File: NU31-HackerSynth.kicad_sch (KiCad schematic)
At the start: 134 parts, among them J1 Conn_02x07_Counter_Clockwise, J2 AudioJack3, J3 Barrel_Jack, J4 AudioJack2_SwitchT, J5 AudioJack2_SwitchT, J6 AudioJack2_SwitchT, Q1 NPN, Q2 NPN, Q3 NPN, Q4 NPN, SW1 SW_Push_DPDT, SW2 SW_SPDT, U1 LM358, U2 LM358, U3 LM358, U4 4017, U5 LM358, U6 LM358, U7 LM358

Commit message: Added eurorack power connector, assigned the footprints and made a (very) draft layout of the board
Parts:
- added J7: Eurorack Power, Connector_PinSocket_2.54mm:PinSocket_2x05_P2.54mm_Vertical, symbol Connector_Generic:Conn_02x05_Odd_Even
- C1, C6: value 50nf -> 50n; footprint (none) -> Capacitor_THT:C_Disc_D5.1mm_W3.2mm_P5.00mm
- C10, C14, C15, C16, C17, C18, C2, C5, C7: footprint (none) -> Capacitor_THT:C_Disc_D5.1mm_W3.2mm_P5.00mm
- C11, C12, C13: footprint (none) -> Capacitor_THT:CP_Radial_D5.0mm_P2.50mm
- C3: value 10nF -> 10n; footprint (none) -> Capacitor_THT:C_Disc_D5.1mm_W3.2mm_P5.00mm
- C4: value 10uF -> 10u; footprint (none) -> Capacitor_THT:C_Disc_D5.1mm_W3.2mm_P5.00mm
- C8: footprint (none) -> Diode_THT:D_A-405_P10.16mm_Horizontal
- C9: value 10 uF -> 10u; footprint (none) -> Capacitor_THT:CP_Radial_D5.0mm_P2.50mm
- D1, D10, D12, D14, D16, D18, D4, D6, D8: footprint (none) -> Diode_THT:D_A-405_P7.62mm_Horizontal
- D11, D13, D15, D17, D3, D5, D7, D9: footprint (none) -> LED_THT:LED_D3.0mm
- D2: value D -> 1N4001; footprint (none) -> Diode_THT:D_A-405_P10.16mm_Horizontal
- J1: footprint (none) -> Connector_PinHeader_2.54mm:PinHeader_2x08_P2.54mm_Vertical; symbol Connector_Generic:Conn_02x08_Counter_Clockwise -> Connector_Generic:Conn_02x08_Odd_Even
- J2: footprint (none) -> AudioJacks:Jack_3.5mm_QingPu_WQP-PJ366ST_Vertical
- J3: footprint (none) -> Connector_BarrelJack:BarrelJack_Wuerth_6941xx301002
- J4, J5, J6: footprint (none) -> AudioJacks:Jack_3.5mm_QingPu_WQP-PJ301M-12_Vertical
- JP1, JP2, JP3, JP4, JP5, JP6, JP7: footprint (none) -> Connector_PinHeader_2.54mm:PinHeader_1x02_P2.54mm_Vertical
- Q1, Q2, Q3, Q4: footprint (none) -> Package_TO_SOT_THT:TO-92L_Inline_Wide
- R1, R10, R11, R12, R13, R14, R15, R16, R17, R18, R19, R2, R20, R21, R22, R23, R24, R25, R26, R27, R28, R29, R3, R30, R31, R32, R33, R34, R35, R36, R37, R38, R39, R4, R40, R41, R42, R43, R44, R45, R46, R47, R48, R49, R5, R50, R51, R52, R53, R54, R55, R56, R57, R58, R6, R7, R8, R9: footprint (none) -> Resistor_THT:R_Axial_DIN0207_L6.3mm_D2.5mm_P10.16mm_Horizontal
- RV1, RV10, RV11, RV12, RV3: footprint (none) -> Potentiometer_THT:Potentiometer_Alpha_RD901F-40-00D_Single_Vertical
- RV13, RV14, RV4, RV5, RV6, RV7, RV8, RV9: footprint (none) -> Potentiometer_THT:Potentiometer_Bourns_PTA2043_Single_Slide
- RV2: footprint (none) -> Potentiometer_THT:Potentiometer_Bourns_3299P_Horizontal
- SW1: value SW_Push_DPDT -> SW_DPDT; footprint (none) -> Button_Switch_THT:SW_CK_JS202011CQN_DPDT_Straight
- SW2: footprint (none) -> Button_Switch_THT:SW_Slide_SPDT_Straight_CK_OS102011MS2Q
- U1, U2, U3, U5, U6, U7: footprint (none) -> Package_DIP:DIP-8_W7.62mm_Socket
- U4: value 4017 -> CD4017; footprint (none) -> Package_DIP:DIP-16_W7.62mm_Socket
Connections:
- net GND: now also J7.3 (Pin_3), J7.4 (Pin_4), J7.5 (Pin_5), J7.6 (Pin_6), J7.7 (Pin_7), J7.8 (Pin_8)
- net at R30.1, RV9.1, U4.1 (Q5): now also J1.10 (Pin_10); no longer J1.12 (Pin_12)
- net at R28.1, RV8.1, U4.10 (Q4): now also J1.8 (Pin_8); no longer J1.13 (Pin_13)
- net at J1.1 (Pin_1), J1.3 (Pin_3), J1.5 (Pin_5)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: now also J1.11 (Pin_11), J1.13 (Pin_13), J1.15 (Pin_15), J1.9 (Pin_9); no longer J1.2 (Pin_2), J1.4 (Pin_4), J1.6 (Pin_6), J1.8 (Pin_8)
- net at R8.1, RV5.1, U4.2 (Q1): now also J1.2 (Pin_2); no longer J1.16 (Pin_16)
- net at R24.1, RV6.1, U4.4 (Q2): now also J1.4 (Pin_4); no longer J1.15 (Pin_15)
- net at R53.1, RV13.1, U4.5 (Q6): now also J1.12 (Pin_12); no longer J1.11 (Pin_11)
- net at R55.1, RV14.1, U4.6 (Q7): now also J1.14 (Pin_14); no longer J1.10 (Pin_10)
- net at R26.1, RV7.1, U4.7 (Q3): now also J1.6 (Pin_6); no longer J1.14 (Pin_14)
- net at U4.9 (Q8): now also J1.16 (Pin_16); no longer J1.9 (Pin_9)
- net at D2.2 (A), J3.2: now also J7.10 (Pin_10), J7.9 (Pin_9)
- no-connect marks 4 -> 6
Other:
- moved on the sheet: C13, D2, J3

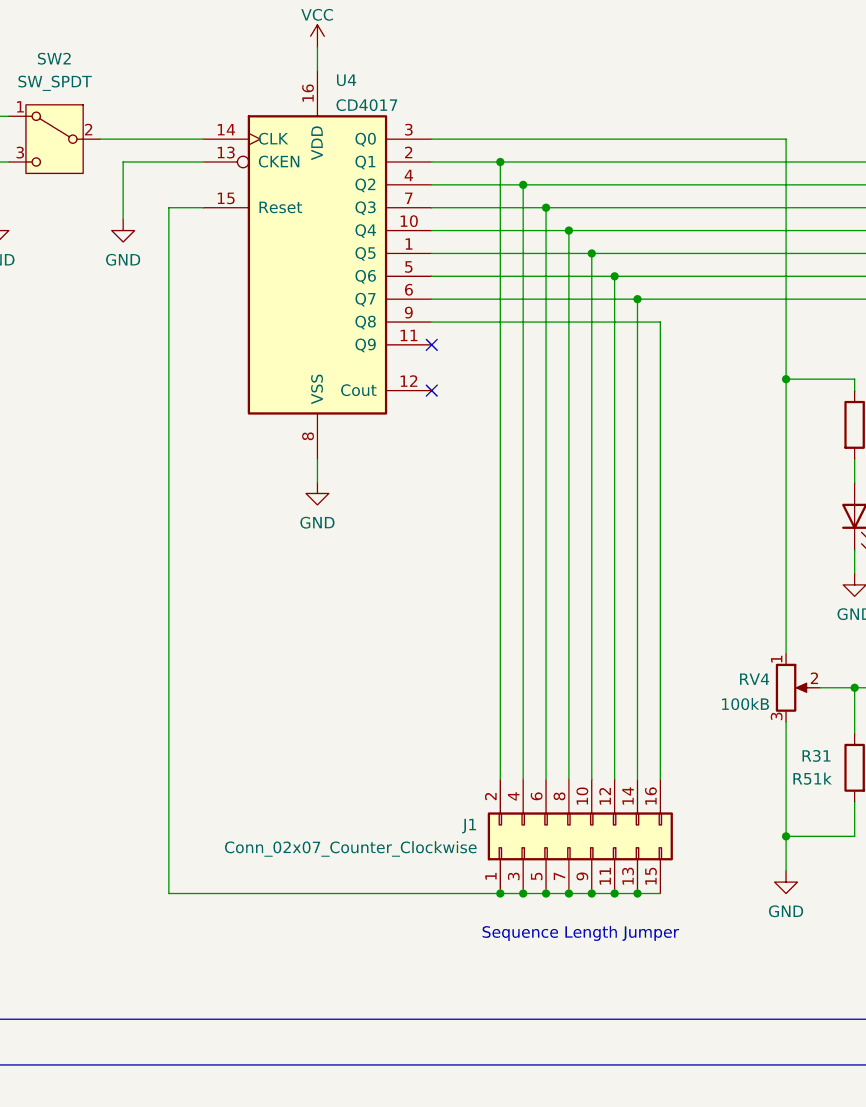
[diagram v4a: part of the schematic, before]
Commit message: Replaced sequence length jumper pins with 8-position switch
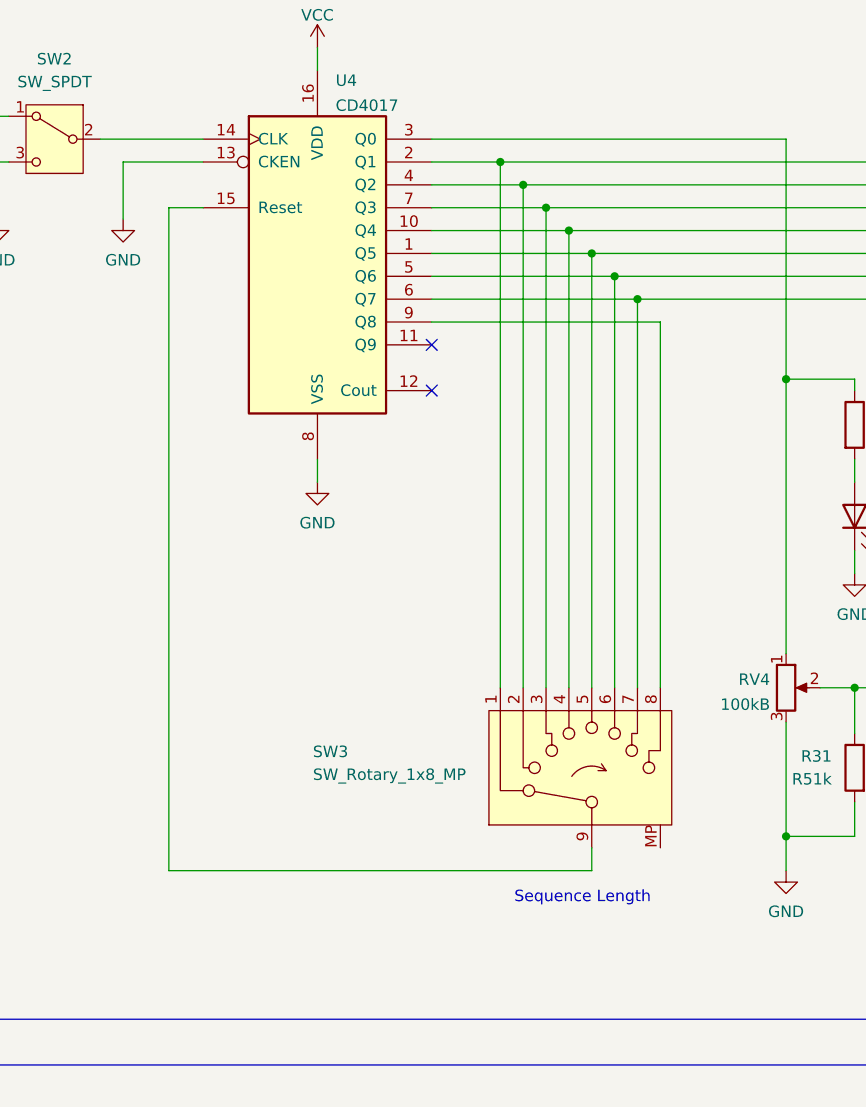
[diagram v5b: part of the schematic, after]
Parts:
- removed J1: Conn_02x07_Counter_Clockwise, Connector_PinHeader_2.54mm:PinHeader_2x08_P2.54mm_Vertical, symbol Connector_Generic:Conn_02x08_Odd_Even
- added SW3: SW_Rotary_1x8_MP, symbol Switch:SW_Rotary_1x8_MP
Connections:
- net at R30.1, RV9.1, U4.1 (Q5): now also SW3.5
- net at R28.1, RV8.1, U4.10 (Q4): now also SW3.4
- net at U4.15 (Reset): now also SW3.9
- net at R8.1, RV5.1, U4.2 (Q1): now also SW3.1
- net at R24.1, RV6.1, U4.4 (Q2): now also SW3.2
- net at R53.1, RV13.1, U4.5 (Q6): now also SW3.6
- net at R55.1, RV14.1, U4.6 (Q7): now also SW3.7
- net at R26.1, RV7.1, U4.7 (Q3): now also SW3.3
- net at U4.9 (Q8): now also SW3.8
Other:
- note added: "Sequence Length"
- note removed: "Sequence Length Jumper"
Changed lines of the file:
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@@
 		)
 	)
-	(text "Sequence Length Jumper"
+	(text "Sequence Length"
 		(exclude_from_sim no)
-		(at 100.33 446.532 0)
+		(at 100.584 442.468 0)
 		(effects
 			(font
@@
 	)
 	(junction
-		(at 106.68 441.96)
-		(diameter 0)
-		(color 0 0 0 0)
-	)
-	(junction
 		(at 327.66 513.08)
 		(diameter 0)
@@
 	)
 	(junction
-		(at 91.44 441.96)
-		(diameter 0)
-		(color 0 0 0 0)
-	)
-	(junction
 		(at 363.22 254)
 		(diameter 0)
@@
 	)
 	(junction
-		(at 96.52 441.96)
-		(diameter 0)
-		(color 0 0 0 0)
-	)
-	(junction
 		(at 123.19 384.81)
 		(diameter 0)
@@
 	)
 	(junction
-		(at 101.6 441.96)
-		(diameter 0)
-		(color 0 0 0 0)
-	)
-	(junction
 		(at 162.56 175.26)
 		(diameter 0)
@@
 	)
 	(junction
-		(at 99.06 441.96)
-		(diameter 0)
-		(color 0 0 0 0)
-	)
-	(junction
 		(at 92.71 285.75)
 		(diameter 0)
@@
 	)
 	(junction
-		(at 104.14 441.96)
-		(diameter 0)
-		(color 0 0 0 0)
-	)
-	(junction
 		(at 342.9 73.66)
 		(diameter 0)
@@
 	)
 	(junction
-		(at 93.98 441.96)
-		(diameter 0)
-		(color 0 0 0 0)
-	)
-	(junction
 		(at 74.93 502.92)
 		(diameter 0)
@@
 	(wire
 		(pts
-			(xy 101.6 441.96) (xy 104.14 441.96)
-		)
-		(stroke
-			(width 0)
-			(type default)
-		)
-	)
-	(wire
-		(pts
 			(xy 341.63 60.96) (xy 342.9 60.96)
 		)
@@
 	(wire
 		(pts
+			(xy 137.16 431.8) (xy 137.16 445.77)
+		)
+		(stroke
+			(width 0)
+			(type default)
+		)
+	)
+	(wire
+		(pts
 			(xy 80.01 285.75) (xy 92.71 285.75)
 		)
@@
 	(wire
 		(pts
-			(xy 99.06 368.3) (xy 99.06 429.26)
+			(xy 99.06 368.3) (xy 99.06 419.1)
 		)
 		(stroke
@@
 	(wire
 		(pts
-			(xy 93.98 363.22) (xy 93.98 429.26)
+			(xy 93.98 363.22) (xy 93.98 419.1)
 		)
 		(stroke
@@
 	(wire
 		(pts
-			(xy 91.44 441.96) (xy 54.61 441.96)
+			(xy 54.61 439.42) (xy 101.6 439.42)
 		)
 		(stroke
@@
 	(wire
 		(pts
-			(xy 96.52 441.96) (xy 99.06 441.96)
-		)
-		(stroke
-			(width 0)
-			(type default)
-		)
-	)
-	(wire
-		(pts
 			(xy 36.83 546.1) (xy 36.83 547.37)
 		)
@@
 	(wire
 		(pts
-			(xy 91.44 441.96) (xy 93.98 441.96)
-		)
-		(stroke
-			(width 0)
-			(type default)
-		)
-	)
-	(wire
-		(pts
 			(xy 340.36 488.95) (xy 345.44 488.95)
 		)
@@
 	(wire
 		(pts
-			(xy 137.16 431.8) (xy 137.16 445.77)
-		)
-		(stroke
-			(width 0)
-			(type default)
-		)
-	)
-	(wire
-		(pts
 			(xy 300.99 53.34) (xy 300.99 68.58)
 		)
@@
 	(wire
 		(pts
+			(xy 101.6 439.42) (xy 101.6 436.88)
+		)
+		(stroke
+			(width 0)
+			(type default)
+		)
+	)
+	(wire
+		(pts
 			(xy 83.82 375.92) (xy 106.68 375.92)
 		)
@@
 	(wire
 		(pts
-			(xy 91.44 360.68) (xy 91.44 429.26)
+			(xy 91.44 360.68) (xy 91.44 419.1)
 		)
 		(stroke
@@
 	(wire
 		(pts
-			(xy 93.98 441.96) (xy 96.52 441.96)
-		)
-		(stroke
-			(width 0)
-			(type default)
-		)
-	)
-	(wire
-		(pts
 			(xy 358.14 419.1) (xy 358.14 424.18)
 		)
@@
 	(wire
 		(pts
-			(xy 106.68 375.92) (xy 106.68 429.26)
+			(xy 106.68 375.92) (xy 106.68 419.1)
 		)
 		(stroke
@@
 	(wire
 		(pts
-			(xy 106.68 441.96) (xy 109.22 441.96)
-		)
-		(stroke
-			(width 0)
-			(type default)
-		)
-	)
-	(wire
-		(pts
 			(xy 226.06 403.86) (xy 226.06 406.4)
 		)
@@
 	(wire
 		(pts
-			(xy 54.61 365.76) (xy 54.61 441.96)
+			(xy 54.61 365.76) (xy 54.61 439.42)
 		)
 		(stroke
@@
 	(wire
 		(pts
-			(xy 96.52 365.76) (xy 96.52 429.26)
+			(xy 96.52 365.76) (xy 96.52 419.1)
 		)
 		(stroke
@@
 	(wire
 		(pts
-			(xy 99.06 441.96) (xy 101.6 441.96)
-		)
-		(stroke
-			(width 0)
-			(type default)
-		)
-	)
-	(wire
-		(pts
 			(xy 77.47 158.75) (xy 93.98 158.75)
 		)
@@
 	(wire
 		(pts
-			(xy 109.22 378.46) (xy 109.22 429.26)
+			(xy 109.22 378.46) (xy 109.22 419.1)
 		)
 		(stroke
@@
 	(wire
 		(pts
-			(xy 104.14 373.38) (xy 104.14 429.26)
+			(xy 104.14 373.38) (xy 104.14 419.1)
 		)
 		(stroke
@@
 	(wire
 		(pts
-			(xy 101.6 370.84) (xy 101.6 429.26)
+			(xy 101.6 370.84) (xy 101.6 419.1)
 		)
 		(stroke
@@
 	(wire
 		(pts
-			(xy 104.14 441.96) (xy 106.68 441.96)
-		)
-		(stroke
-			(width 0)
-			(type default)
-		)
-	)
-	(wire
-		(pts
 			(xy 311.15 53.34) (xy 308.61 53.34)
 		)
@@
 	)
 	(symbol
-		(lib_id "Connector_Generic:Conn_02x08_Odd_Even")
-		(at 99.06 436.88 90)
-		(unit 1)
-		(exclude_from_sim no)
-		(in_bom yes)
-		(on_board yes)
-		(dnp no)
-		(fields_autoplaced yes)
-		(property "Reference" "J1"
-			(at 88.9 434.3399 90)
-			(effects
-				(font
-					(size 1.27 1.27)
-				)
-				(justify left)
-			)
-		)
-		(property "Value" "Conn_02x07_Counter_Clockwise"
-			(at 88.9 436.8799 90)
-			(effects
-				(font
-					(size 1.27 1.27)
-				)
-				(justify left)
-			)
-		)
-		(property "Footprint" "Connector_PinHeader_2.54mm:PinHeader_2x08_P2.54mm_Vertical"
-			(at 99.06 436.88 0)
-			(effects
-				(font
-					(size 1.27 1.27)
-				)
-				(hide yes)
-			)
-		)
-		(property "Datasheet" "~"
-			(at 99.06 436.88 0)
-			(effects
-				(font
-					(size 1.27 1.27)
-				)
-				(hide yes)
-			)
-		)
-		(property "Description" "Generic connector, double row, 02x08, odd/even pin numbering scheme (row 1 odd numbers, row 2 even numbers), script generated (kicad-library-utils/schlib/autogen/connector/)"
-			(at 99.06 436.88 0)
-			(effects
-				(font
-					(size 1.27 1.27)
-				)
-				(hide yes)
-			)
-		)
-		(pin "3"
-		)
-		(pin "10"
-		)
-		(pin "6"
-		)
-		(pin "5"
-		)
-		(pin "9"
-		)
-		(pin "4"
-		)
-		(pin "1"
-		)
-		(pin "12"
-		)
-		(pin "13"
-		)
-		(pin "14"
-		)
-		(pin "8"
-		)
-		(pin "11"
-		)
-		(pin "2"
-		)
-		(pin "7"
-		)
-		(pin "16"
-		)
-		(pin "15"
-		)
-		(instances
-			(project ""
-				(path "/151a4108-ccd8-4864-9fa1-a2e140a3decb"
-					(reference "J1")
-					(unit 1)
-				)
-			)
-		)
-	)
-	(symbol
 		(lib_id "Device:R")
 		(at 351.79 389.89 0)
@@
 					(unit 1)
 				)
+			)
+		)
+	)
+	(symbol
+		(lib_id "Switch:SW_Rotary_1x8_MP")
+		(at 101.6 426.72 90)
+		(unit 1)
+		(exclude_from_sim no)
+		(in_bom yes)
+		(on_board yes)
+		(dnp no)
+		(property "Reference" "SW3"
+			(at 70.612 426.212 90)
+			(effects
+				(font
+					(size 1.27 1.27)
+				)
+				(justify right)
+			)
+		)
+		(property "Value" "SW_Rotary_1x8_MP"
+			(at 70.612 428.752 90)
+			(effects
+				(font
+					(size 1.27 1.27)
+				)
+				(justify right)
+			)
+		)
+		(property "Footprint" ""
+			(at 101.6 427.99 0)
+			(effects
+				(font
+					(size 1.27 1.27)
+				)
+				(hide yes)
+			)
+		)
+		(property "Datasheet" "~"
+			(at 101.6 427.99 0)
+			(effects
+				(font
+					(size 1.27 1.27)
+				)
+				(hide yes)
+			)
+		)
+		(property "Description" "Rotary switch 1x8, SP8T with mount point"
+			(at 101.6 426.72 0)
+			(effects
+				(font
+					(size 1.27 1.27)
+				)
+				(hide yes)
+			)
+		)
+		(pin "MP"
+		)
+		(pin "1"
+		)
+		(pin "9"
+		)
+		(pin "3"
+		)
+		(pin "6"
+		)
+		(pin "5"
+		)
+		(pin "2"
+		)
+		(pin "4"
+		)
+		(pin "8"
+		)
+		(pin "7"
+		)
+		(instances
+			(project "NU31-HackerSynth"
+				(path "/151a4108-ccd8-4864-9fa1-a2e140a3decb"
+					(reference "SW3")
+					(unit 1)
+				)

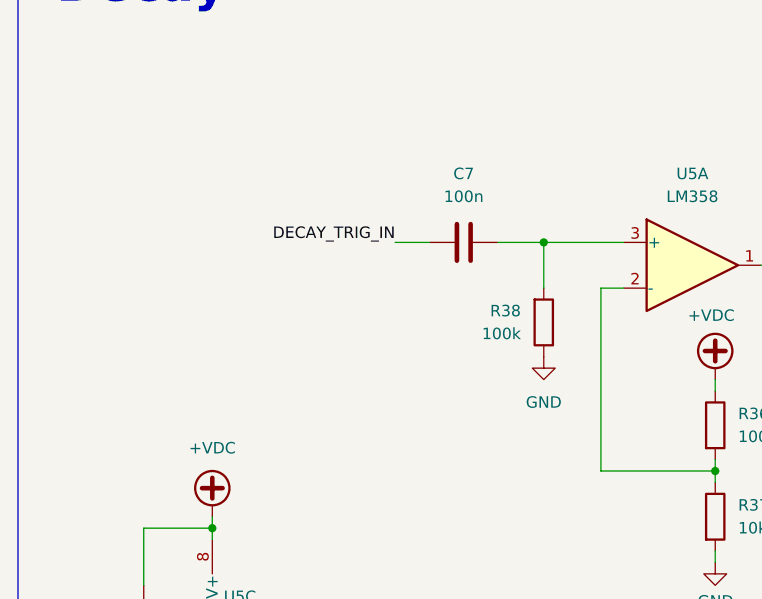
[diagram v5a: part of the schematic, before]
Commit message: Added diode to filter out negatvie voltages in decay circuit input
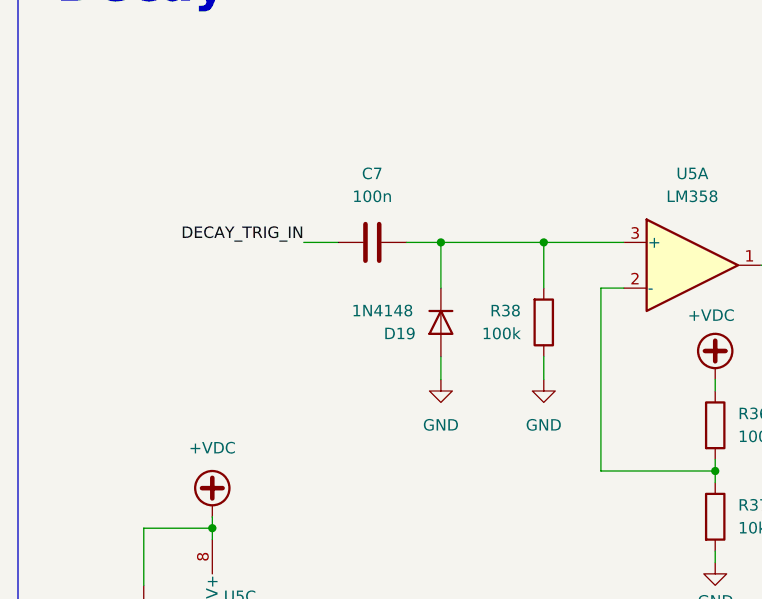
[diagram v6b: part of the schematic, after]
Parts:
- added D19: 1N4148, Diode_THT:D_A-405_P7.62mm_Horizontal, symbol Device:D
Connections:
- net GND: now also D19.2 (A)
- net at C7.2, R38.2, U5.3 (+): now also D19.1 (K)
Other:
- moved on the sheet: C7
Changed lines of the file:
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@@
 	)
 	(junction
+		(at 62.23 260.35)
+		(diameter 0)
+		(color 0 0 0 0)
+	)
+	(junction
 		(at 328.93 45.72)
 		(diameter 0)
@@
 	(wire
 		(pts
+			(xy 62.23 275.59) (xy 62.23 273.05)
+		)
+		(stroke
+			(width 0)
+			(type default)
+		)
+	)
+	(wire
+		(pts
 			(xy 222.25 419.1) (xy 226.06 419.1)
 		)
@@
 	(wire
 		(pts
+			(xy 73.66 275.59) (xy 73.66 273.05)
+		)
+		(stroke
+			(width 0)
+			(type default)
+		)
+	)
+	(wire
+		(pts
 			(xy 137.16 431.8) (xy 137.16 445.77)
 		)
@@
 	(wire
 		(pts
+			(xy 62.23 260.35) (xy 73.66 260.35)
+		)
+		(stroke
+			(width 0)
+			(type default)
+		)
+	)
+	(wire
+		(pts
 			(xy 99.06 59.69) (xy 99.06 57.15)
 		)
@@
 	(wire
 		(pts
-			(xy 57.15 260.35) (xy 60.96 260.35)
+			(xy 46.99 260.35) (xy 50.8 260.35)
 		)
 		(stroke
@@
 	(wire
 		(pts
+			(xy 62.23 265.43) (xy 62.23 260.35)
+		)
+		(stroke
+			(width 0)
+			(type default)
+		)
+	)
+	(wire
+		(pts
 			(xy 340.36 488.95) (xy 345.44 488.95)
 		)
@@
 	(wire
 		(pts
-			(xy 68.58 260.35) (xy 73.66 260.35)
+			(xy 58.42 260.35) (xy 62.23 260.35)
 		)
 		(stroke
@@
 	)
 	(label "DECAY_TRIG_IN"
-		(at 57.15 260.35 180)
+		(at 46.99 260.35 180)
 		(effects
 			(font
@@
 	)
 	(symbol
+		(lib_id "Device:D")
+		(at 62.23 269.24 90)
+		(mirror x)
+		(unit 1)
+		(exclude_from_sim no)
+		(in_bom yes)
+		(on_board yes)
+		(dnp no)
+		(property "Reference" "D19"
+			(at 55.88 270.51 90)
+			(effects
+				(font
+					(size 1.27 1.27)
+				)
+				(justify right)
+			)
+		)
+		(property "Value" "1N4148"
+			(at 52.324 267.97 90)
+			(effects
+				(font
+					(size 1.27 1.27)
+				)
+				(justify right)
+			)
+		)
+		(property "Footprint" "Diode_THT:D_A-405_P7.62mm_Horizontal"
+			(at 62.23 269.24 0)
+			(effects
+				(font
+					(size 1.27 1.27)
+				)
+				(hide yes)
+			)
+		)
+		(property "Datasheet" "~"
+			(at 62.23 269.24 0)
+			(effects
+				(font
+					(size 1.27 1.27)
+				)
+				(hide yes)
+			)
+		)
+		(property "Description" ""
+			(at 62.23 269.24 0)
+			(effects
+				(font
+					(size 1.27 1.27)
+				)
+			)
+		)
+		(pin "1"
+		)
+		(pin "2"
+		)
+		(instances
+			(project "NU31-HackerSynth"
+				(path "/151a4108-ccd8-4864-9fa1-a2e140a3decb"
+					(reference "D19")
+					(unit 1)
+				)
+			)
+		)
+	)
+	(symbol
 		(lib_id "power:+VDC")
 		(at 36.83 187.96 0)
@@
 	)
 	(symbol
+		(lib_id "power:GND")
+		(at 62.23 275.59 0)
+		(unit 1)
+		(exclude_from_sim no)
+		(in_bom yes)
+		(on_board yes)
+		(dnp no)
+		(fields_autoplaced yes)
+		(property "Reference" "#PWR059"
+			(at 62.23 281.94 0)
+			(effects
+				(font
+					(size 1.27 1.27)
+				)
+				(hide yes)
+			)
+		)
+		(property "Value" "GND"
+			(at 62.23 280.67 0)
+			(effects
+				(font
+					(size 1.27 1.27)
+				)
+			)
+		)
+		(property "Footprint" ""
+			(at 62.23 275.59 0)
+			(effects
+				(font
+					(size 1.27 1.27)
+				)
+				(hide yes)
+			)
+		)
+		(property "Datasheet" ""
+			(at 62.23 275.59 0)
+			(effects
+				(font
+					(size 1.27 1.27)
+				)
+				(hide yes)
+			)
+		)
+		(property "Description" "Power symbol creates a global label with name \"GND\" , ground"
+			(at 62.23 275.59 0)
+			(effects
+				(font
+					(size 1.27 1.27)
+				)
+				(hide yes)
+			)
+		)
+		(pin "1"
+		)
+		(instances
+			(project "NU31-HackerSynth"
+				(path "/151a4108-ccd8-4864-9fa1-a2e140a3decb"
+					(reference "#PWR059")
+					(unit 1)
+				)
+			)
+		)
+	)
+	(symbol
 		(lib_id "Device:R")
 		(at 256.54 389.89 0)
@@
 	(symbol
 		(lib_id "Device:C")
-		(at 64.77 260.35 90)
+		(at 54.61 260.35 90)
 		(unit 1)
 		(exclude_from_sim no)
@@
 		(fields_autoplaced yes)
 		(property "Reference" "C7"
-			(at 64.77 252.73 90)
+			(at 54.61 252.73 90)
 			(effects
 				(font
@@
 		)
 		(property "Value" "100n"
-			(at 64.77 255.27 90)
+			(at 54.61 255.27 90)
 			(effects
 				(font
@@
 		)
 		(property "Footprint" "Capacitor_THT:C_Disc_D5.1mm_W3.2mm_P5.00mm"
-			(at 68.58 259.3848 0)
+			(at 58.42 259.3848 0)
 			(effects
 				(font
@@
 		)
 		(property "Datasheet" "~"
-			(at 64.77 260.35 0)
+			(at 54.61 260.35 0)
 			(effects
 				(font
@@
 		)
 		(property "Description" "Unpolarized capacitor"
-			(at 64.77 260.35 0)
+			(at 54.61 260.35 0)
 			(effects
 				(font
@@
 	(symbol
 		(lib_id "power:GND")
-		(at 73.66 273.05 0)
+		(at 73.66 275.59 0)
 		(unit 1)
 		(exclude_from_sim no)
@@
 		(fields_autoplaced yes)
 		(property "Reference" "#PWR032"
-			(at 73.66 279.4 0)
+			(at 73.66 281.94 0)
 			(effects
 				(font
@@
 		)
 		(property "Value" "GND"
-			(at 73.66 278.13 0)
+			(at 73.66 280.67 0)
 			(effects
 				(font
@@
 		)
 		(property "Footprint" ""
-			(at 73.66 273.05 0)
+			(at 73.66 275.59 0)
 			(effects
 				(font
@@
 		)
 		(property "Datasheet" ""
-			(at 73.66 273.05 0)
+			(at 73.66 275.59 0)
 			(effects
 				(font
@@
 		)
 		(property "Description" "Power symbol creates a global label with name \"GND\" , ground"
-			(at 73.66 273.05 0)
+			(at 73.66 275.59 0)
 			(effects
 				(font
